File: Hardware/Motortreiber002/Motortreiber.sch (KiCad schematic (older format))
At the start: 15 parts, among them J1201 Screw_Terminal_01x04, J1202 Screw_Terminal_01x04, U1201 DRV8823

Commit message: 16 Motortreiber
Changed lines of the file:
@@
 $Descr A4 11693 8268
 encoding utf-8
-Sheet 8 19
+Sheet 7 19
 Title ""
 Date ""
@@
 AR Path="/5CC752B0/5CAFBB89" Ref="#PWR?"  Part="1"
 AR Path="/5CC4B548/5CAFBB89" Ref="#PWR02101"  Part="1"
-F 0 "#PWR01901" H 1950 1900 50  0001 C CNN
+F 0 "#PWR02101" H 1950 1900 50  0001 C CNN
 F 1 "+28V" H 1965 2223 50  0000 C CNN
 F 2 "" H 2200 2100 50  0001 C CNN
@@
 AR Path="/5CC752B0/5CA10EF0" Ref="U?"  Part="1"
 AR Path="/5CC4B548/5CA10EF0" Ref="U2101"  Part="1"
-F 0 "U1901" H 4650 5065 50  0000 C CNN
+F 0 "U1001" H 4650 5065 50  0000 C CNN
 F 1 "DRV8823" H 4650 4974 50  0000 C CNN
 F 2 "Package_SO:TSSOP-48_6.1x12.5mm_P0.5mm" V 4550 3350 50  0001 C CNN
@@
 AR Path="/5CC752B0/5CA5AEA1" Ref="J?"  Part="1"
 AR Path="/5CC4B548/5CA5AEA1" Ref="J2101"  Part="1"
-F 0 "J1901" V 4564 1312 50  0000 R CNN
+F 0 "J1001" V 4564 1312 50  0000 R CNN
 F 1 "Screw_Terminal_01x04" V 4473 1312 50  0000 R CNN
 F 2 "Connector_Phoenix_MC_HighVoltage:PhoenixContact_MCV_1,5_4-G-5.08_1x04_P5.08mm_Vertical" H 4600 1600 50  0001 C CNN
@@
 AR Path="/5CC752B0/5CA5CF1C" Ref="J?"  Part="1"
 AR Path="/5CC4B548/5CA5CF1C" Ref="J2102"  Part="1"
-F 0 "J1902" V 4522 5430 50  0000 L CNN
+F 0 "J1002" V 4522 5430 50  0000 L CNN
 F 1 "Screw_Terminal_01x04" V 4613 5430 50  0000 L CNN
 F 2 "Connector_Phoenix_MC_HighVoltage:PhoenixContact_MCV_1,5_4-G-5.08_1x04_P5.08mm_Vertical" H 4650 5250 50  0001 C CNN
@@
 AR Path="/5CC752B0/5CB597A7" Ref="#PWR?"  Part="1"
 AR Path="/5CC4B548/5CB597A7" Ref="#PWR02111"  Part="1"
-F 0 "#PWR01911" H 5600 3300 50  0001 C CNN
+F 0 "#PWR02111" H 5600 3300 50  0001 C CNN
 F 1 "GND" H 5605 3377 50  0000 C CNN
 F 2 "" H 5600 3550 50  0001 C CNN
@@
 AR Path="/5CC752B0/5CB5E84A" Ref="#PWR?"  Part="1"
 AR Path="/5CC4B548/5CB5E84A" Ref="#PWR02110"  Part="1"
-F 0 "#PWR01910" H 3800 3300 50  0001 C CNN
+F 0 "#PWR02110" H 3800 3300 50  0001 C CNN
 F 1 "GND" H 3805 3377 50  0000 C CNN
 F 2 "" H 3800 3550 50  0001 C CNN
@@
 AR Path="/5CC752B0/5CB640E6" Ref="R?"  Part="1"
 AR Path="/5CC4B548/5CB640E6" Ref="R2102"  Part="1"
-F 0 "R1902" V 3193 2600 50  0000 C CNN
+F 0 "R1002" V 3193 2600 50  0000 C CNN
 F 1 "0R5" V 3284 2600 50  0000 C CNN
 F 2 "Resistor_THT:R_Axial_DIN0411_L9.9mm_D3.6mm_P5.08mm_Vertical" V 3330 2600 50  0001 C CNN
@@
 AR Path="/5CC752B0/5CB64BF2" Ref="R?"  Part="1"
 AR Path="/5CC4B548/5CB64BF2" Ref="R2101"  Part="1"
-F 0 "R1901" V 2643 4900 50  0000 C CNN
+F 0 "R1001" V 2643 4900 50  0000 C CNN
 F 1 "0R5" V 2734 4900 50  0000 C CNN
 F 2 "Resistor_THT:R_Axial_DIN0411_L9.9mm_D3.6mm_P5.08mm_Vertical" V 2780 4900 50  0001 C CNN
@@
 AR Path="/5CC752B0/5CB65616" Ref="R?"  Part="1"
 AR Path="/5CC4B548/5CB65616" Ref="R2104"  Part="1"
-F 0 "R1904" V 5493 4500 50  0000 C CNN
+F 0 "R1004" V 5493 4500 50  0000 C CNN
 F 1 "0R5" V 5584 4500 50  0000 C CNN
 F 2 "Resistor_THT:R_Axial_DIN0411_L9.9mm_D3.6mm_P5.08mm_Vertical" V 5630 4500 50  0001 C CNN
@@
 AR Path="/5CC752B0/5CB65C0C" Ref="R?"  Part="1"
 AR Path="/5CC4B548/5CB65C0C" Ref="R2103"  Part="1"
-F 0 "R1903" V 5493 2400 50  0000 C CNN
+F 0 "R1003" V 5493 2400 50  0000 C CNN
 F 1 "0R5" V 5584 2400 50  0000 C CNN
 F 2 "Resistor_THT:R_Axial_DIN0411_L9.9mm_D3.6mm_P5.08mm_Vertical" V 5630 2400 50  0001 C CNN
@@
 AR Path="/5CC752B0/5CB99402" Ref="#PWR?"  Part="1"
 AR Path="/5CC4B548/5CB99402" Ref="#PWR02108"  Part="1"
-F 0 "#PWR01908" H 3200 2400 50  0001 C CNN
+F 0 "#PWR02108" H 3200 2400 50  0001 C CNN
 F 1 "GND" H 3205 2477 50  0000 C CNN
 F 2 "" H 3200 2650 50  0001 C CNN
@@
 AR Path="/5CC752B0/5CB99CB4" Ref="#PWR?"  Part="1"
 AR Path="/5CC4B548/5CB99CB4" Ref="#PWR02105"  Part="1"
-F 0 "#PWR01905" H 2650 4700 50  0001 C CNN
+F 0 "#PWR02105" H 2650 4700 50  0001 C CNN
 F 1 "GND" H 2655 4777 50  0000 C CNN
 F 2 "" H 2650 4950 50  0001 C CNN
@@
 AR Path="/5CC752B0/5CB99D3F" Ref="#PWR?"  Part="1"
 AR Path="/5CC4B548/5CB99D3F" Ref="#PWR02113"  Part="1"
-F 0 "#PWR01913" H 5900 4300 50  0001 C CNN
+F 0 "#PWR02113" H 5900 4300 50  0001 C CNN
 F 1 "GND" H 5905 4377 50  0000 C CNN
 F 2 "" H 5900 4550 50  0001 C CNN
@@
 AR Path="/5CC752B0/5CB9A10F" Ref="#PWR?"  Part="1"
 AR Path="/5CC4B548/5CB9A10F" Ref="#PWR02112"  Part="1"
-F 0 "#PWR01912" H 5900 2200 50  0001 C CNN
+F 0 "#PWR02112" H 5900 2200 50  0001 C CNN
 F 1 "GND" H 5905 2277 50  0000 C CNN
 F 2 "" H 5900 2450 50  0001 C CNN
@@
 AR Path="/5CC752B0/5CBA36F8" Ref="C?"  Part="1"
 AR Path="/5CC4B548/5CBA36F8" Ref="C2102"  Part="1"
-F 0 "C1902" H 2715 3596 50  0000 L CNN
+F 0 "C1002" H 2715 3596 50  0000 L CNN
 F 1 "100nF 6,3V" H 2715 3505 50  0000 L CNN
 F 2 "Capacitor_SMD:C_0201_0603Metric" H 2638 3400 50  0001 C CNN
@@
 AR Path="/5CC752B0/5CBA4977" Ref="#PWR?"  Part="1"
 AR Path="/5CC4B548/5CBA4977" Ref="#PWR02103"  Part="1"
-F 0 "#PWR01903" H 2600 3550 50  0001 C CNN
+F 0 "#PWR02103" H 2600 3550 50  0001 C CNN
 F 1 "GND" H 2605 3627 50  0000 C CNN
 F 2 "" H 2600 3800 50  0001 C CNN
@@
 AR Path="/5CC752B0/5CBD32BF" Ref="C?"  Part="1"
 AR Path="/5CC4B548/5CBD32BF" Ref="C2107"  Part="1"
-F 0 "C1907" H 3565 2896 50  0000 L CNN
+F 0 "C1007" H 3565 2896 50  0000 L CNN
 F 1 "10nF 50V" H 3565 2805 50  0000 L CNN
 F 2 "Capacitor_SMD:C_0402_1005Metric" H 3488 2700 50  0001 C CNN
@@
 AR Path="/5CC752B0/5CBD3B7F" Ref="C?"  Part="1"
 AR Path="/5CC4B548/5CBD3B7F" Ref="C2108"  Part="1"
-F 0 "C1908" H 3565 3296 50  0000 L CNN
+F 0 "C1008" H 3565 3296 50  0000 L CNN
 F 1 "100nF 16V" H 3565 3205 50  0000 L CNN
 F 2 "Capacitor_SMD:C_0402_1005Metric" H 3488 3100 50  0001 C CNN
@@
 AR Path="/5CC752B0/5CC199C8" Ref="C?"  Part="1"
 AR Path="/5CC4B548/5CC199C8" Ref="C2101"  Part="1"
-F 0 "C1901" H 2265 2296 50  0000 L CNN
+F 0 "C1001" H 2265 2296 50  0000 L CNN
 F 1 "100nF" H 2265 2205 50  0000 L CNN
 F 2 "Capacitor_THT:C_Disc_D8.0mm_W5.0mm_P5.00mm" H 2188 2100 50  0001 C CNN
@@
 AR Path="/5CC752B0/5CC1A57F" Ref="C?"  Part="1"
 AR Path="/5CC4B548/5CC1A57F" Ref="C2103"  Part="1"
-F 0 "C1903" H 2765 2296 50  0000 L CNN
+F 0 "C1003" H 2765 2296 50  0000 L CNN
 F 1 "100nF" H 2765 2205 50  0000 L CNN
 F 2 "Capacitor_THT:C_Disc_D8.0mm_W5.0mm_P5.00mm" H 2688 2100 50  0001 C CNN
@@
 AR Path="/5CC752B0/5CC1B08E" Ref="#PWR?"  Part="1"
 AR Path="/5CC4B548/5CC1B08E" Ref="#PWR02102"  Part="1"
-F 0 "#PWR01902" H 2150 2150 50  0001 C CNN
+F 0 "#PWR02102" H 2150 2150 50  0001 C CNN
 F 1 "GND" H 2155 2227 50  0000 C CNN
 F 2 "" H 2150 2400 50  0001 C CNN
@@
 AR Path="/5CC752B0/5CC1B34B" Ref="#PWR?"  Part="1"
 AR Path="/5CC4B548/5CC1B34B" Ref="#PWR02104"  Part="1"
-F 0 "#PWR01904" H 2650 2150 50  0001 C CNN
+F 0 "#PWR02104" H 2650 2150 50  0001 C CNN
 F 1 "GND" H 2655 2227 50  0000 C CNN
 F 2 "" H 2650 2400 50  0001 C CNN
@@
 AR Path="/5CC752B0/5CC1B722" Ref="C?"  Part="1"
 AR Path="/5CC4B548/5CC1B722" Ref="C2105"  Part="1"
-F 0 "C1905" H 3268 2296 50  0000 L CNN
+F 0 "C1005" H 3268 2296 50  0000 L CNN
 F 1 "33uF 35V" H 3268 2205 50  0000 L CNN
 F 2 "Capacitor_THT:CP_Radial_D5.0mm_P2.00mm" H 3188 2100 50  0001 C CNN
@@
 AR Path="/5CC752B0/5CC1C247" Ref="#PWR?"  Part="1"
 AR Path="/5CC4B548/5CC1C247" Ref="#PWR02107"  Part="1"
-F 0 "#PWR01907" H 3150 2150 50  0001 C CNN
+F 0 "#PWR02107" H 3150 2150 50  0001 C CNN
 F 1 "GND" H 3155 2227 50  0000 C CNN
 F 2 "" H 3150 2400 50  0001 C CNN
@@
 AR Path="/5CC7522D/5CCBF437" Ref="C2206"  Part="1"
 AR Path="/5CC4B548/5CCBF437" Ref="C2106"  Part="1"
-F 0 "C1906" H 3515 4396 50  0000 L CNN
+F 0 "C1006" H 3515 4396 50  0000 L CNN
 F 1 "1nF 25V" H 3515 4305 50  0000 L CNN
 F 2 "Capacitor_SMD:C_0201_0603Metric" H 3438 4200 50  0001 C CNN
@@
 AR Path="/5CC7522D/5CCBF8F9" Ref="C2204"  Part="1"
 AR Path="/5CC4B548/5CCBF8F9" Ref="C2104"  Part="1"
-F 0 "C1904" H 3165 4396 50  0000 L CNN
+F 0 "C1004" H 3165 4396 50  0000 L CNN
 F 1 "1nF 25V" H 3165 4305 50  0000 L CNN
 F 2 "Capacitor_SMD:C_0201_0603Metric" H 3088 4200 50  0001 C CNN
@@
 AR Path="/5CC7522D/5CCBFD0C" Ref="#PWR02209"  Part="1"
 AR Path="/5CC4B548/5CCBFD0C" Ref="#PWR02109"  Part="1"
-F 0 "#PWR01909" H 3400 4250 50  0001 C CNN
+F 0 "#PWR02109" H 3400 4250 50  0001 C CNN
 F 1 "GND" H 3405 4327 50  0000 C CNN
 F 2 "" H 3400 4500 50  0001 C CNN
@@
 AR Path="/5CC7522D/5CCBFDA5" Ref="#PWR02206"  Part="1"
 AR Path="/5CC4B548/5CCBFDA5" Ref="#PWR02106"  Part="1"
-F 0 "#PWR01906" H 3050 4250 50  0001 C CNN
+F 0 "#PWR02106" H 3050 4250 50  0001 C CNN
 F 1 "GND" H 3055 4327 50  0000 C CNN
 F 2 "" H 3050 4500 50  0001 C CNN
@@
 Connection ~ 6200 2700
 Text HLabel 6750 2700 2    50   Input ~ 0
-Steuer
+Steuer[0..6]
 Text HLabel 5800 4100 2    50   Input ~ 0
 Uebernahme

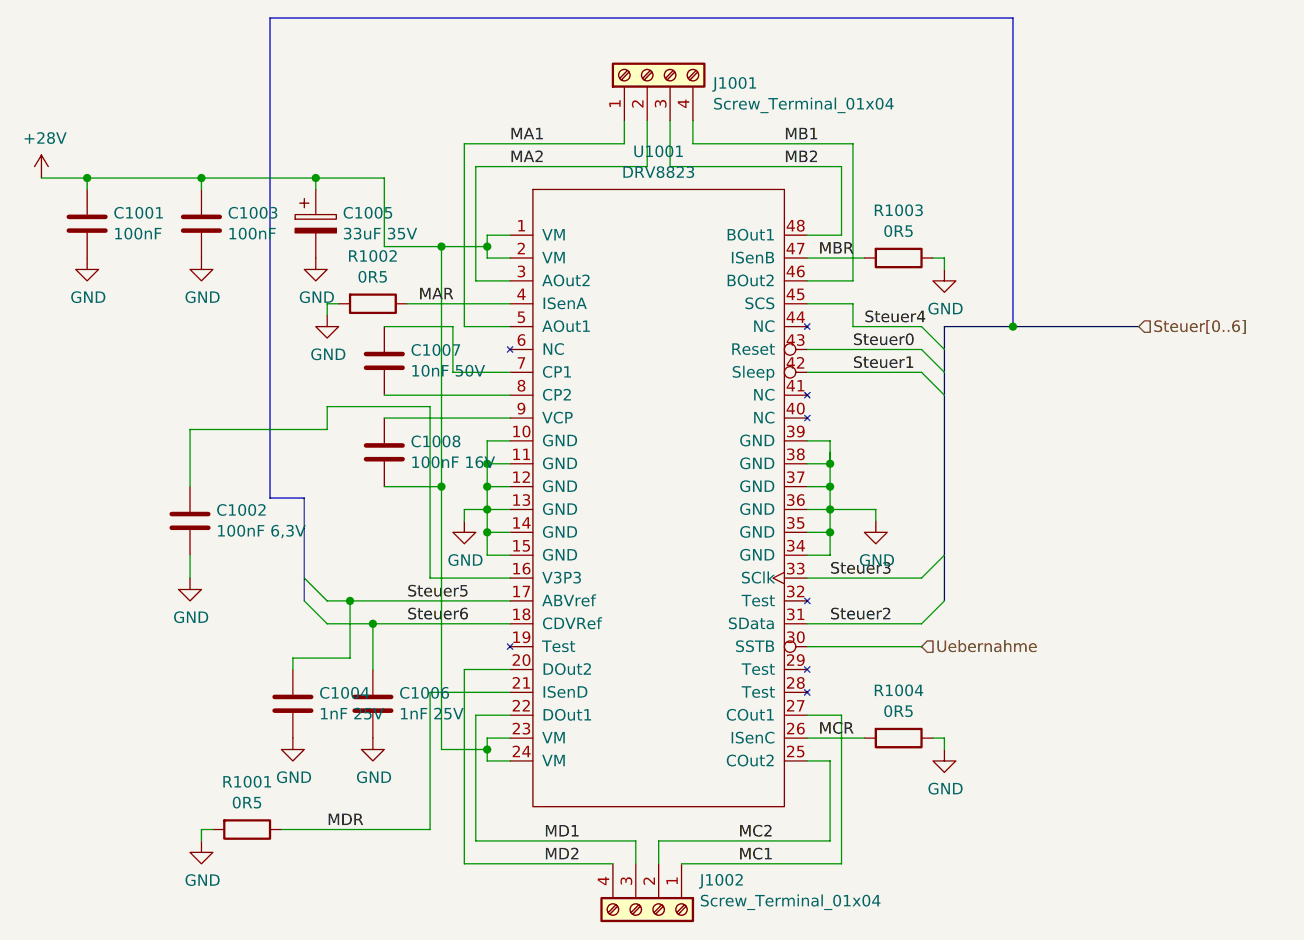
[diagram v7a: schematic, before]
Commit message: Layout 16 Motortreiber grob fertig
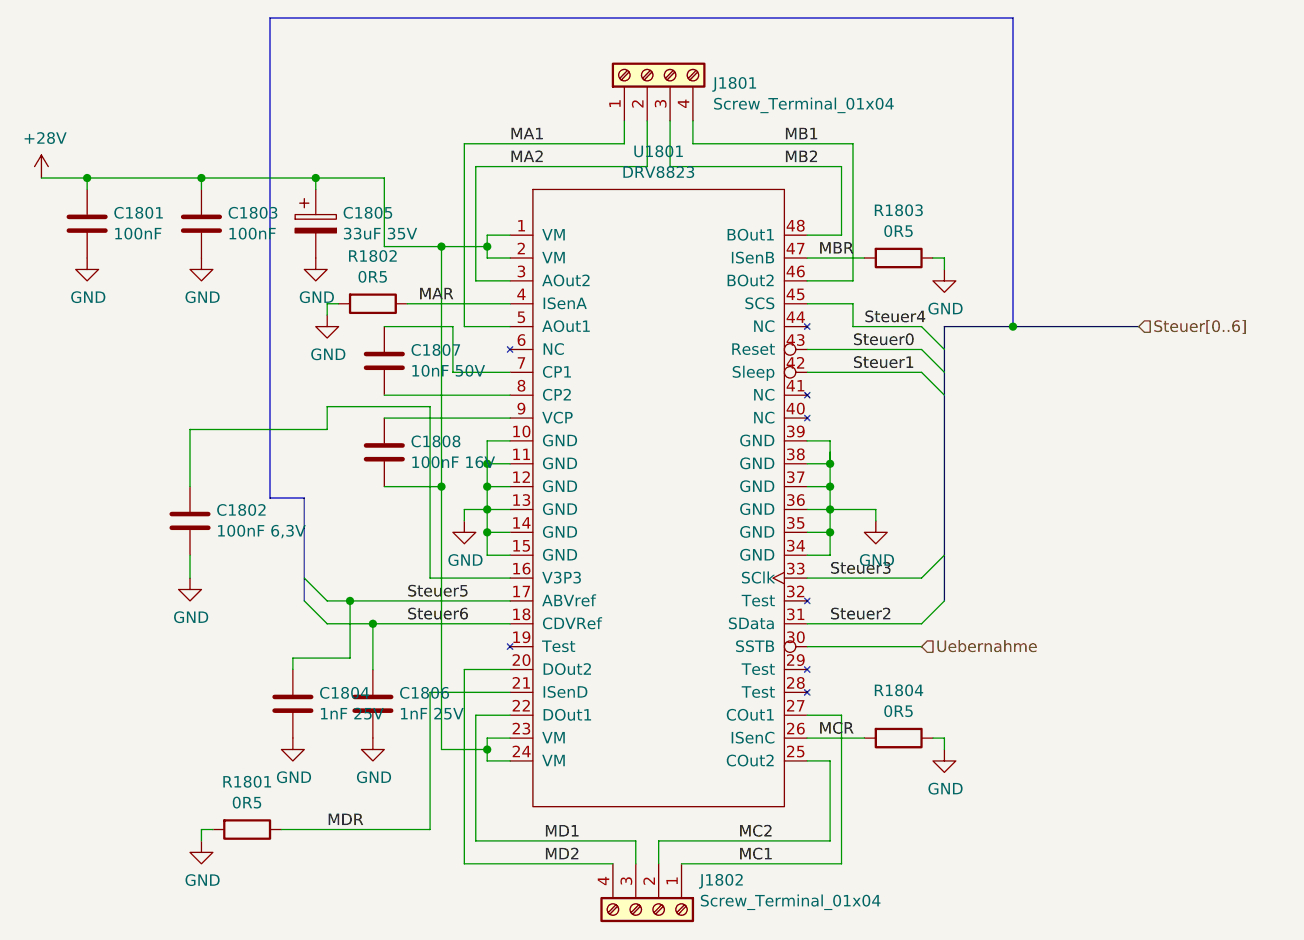
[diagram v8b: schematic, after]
